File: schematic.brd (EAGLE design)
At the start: 100 x 80 mm, 24 parts, among them IC1 ATMEGA168-20P, IC2 7805T, IC3 REG1117

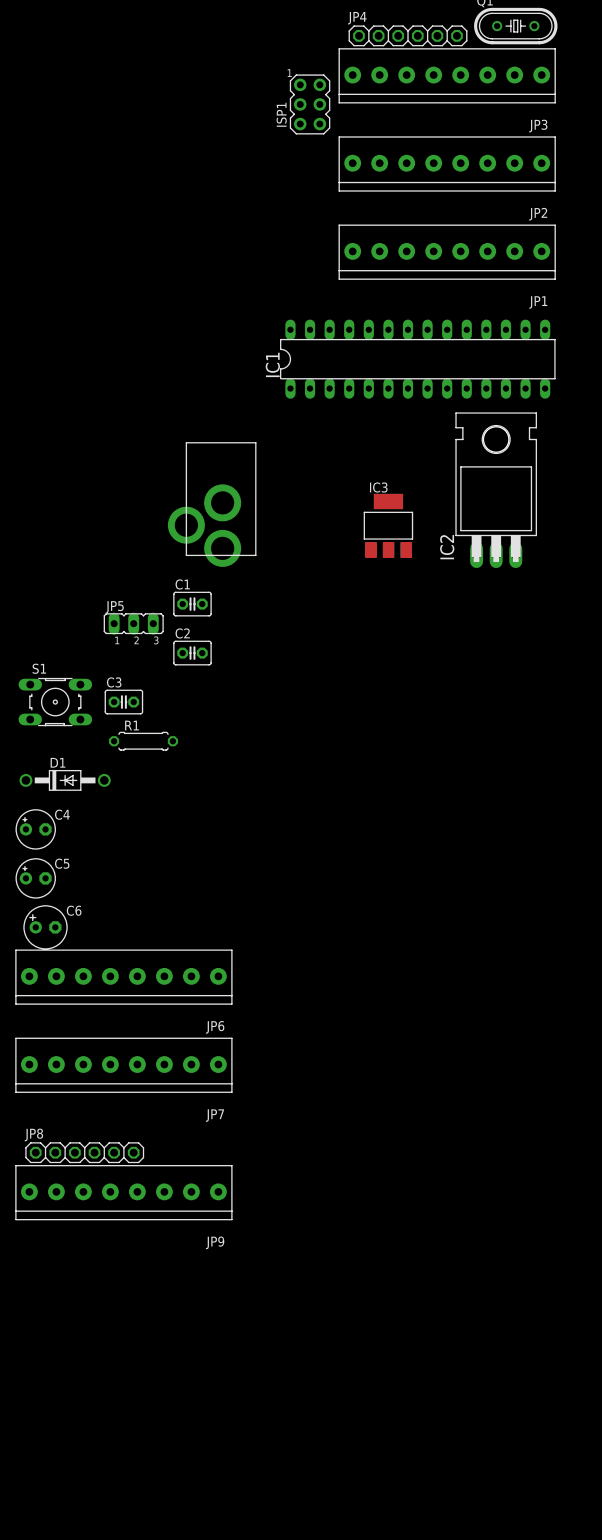
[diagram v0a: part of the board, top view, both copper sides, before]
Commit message: Small fixes
Added a serial port header and LEDs for on and pin 13
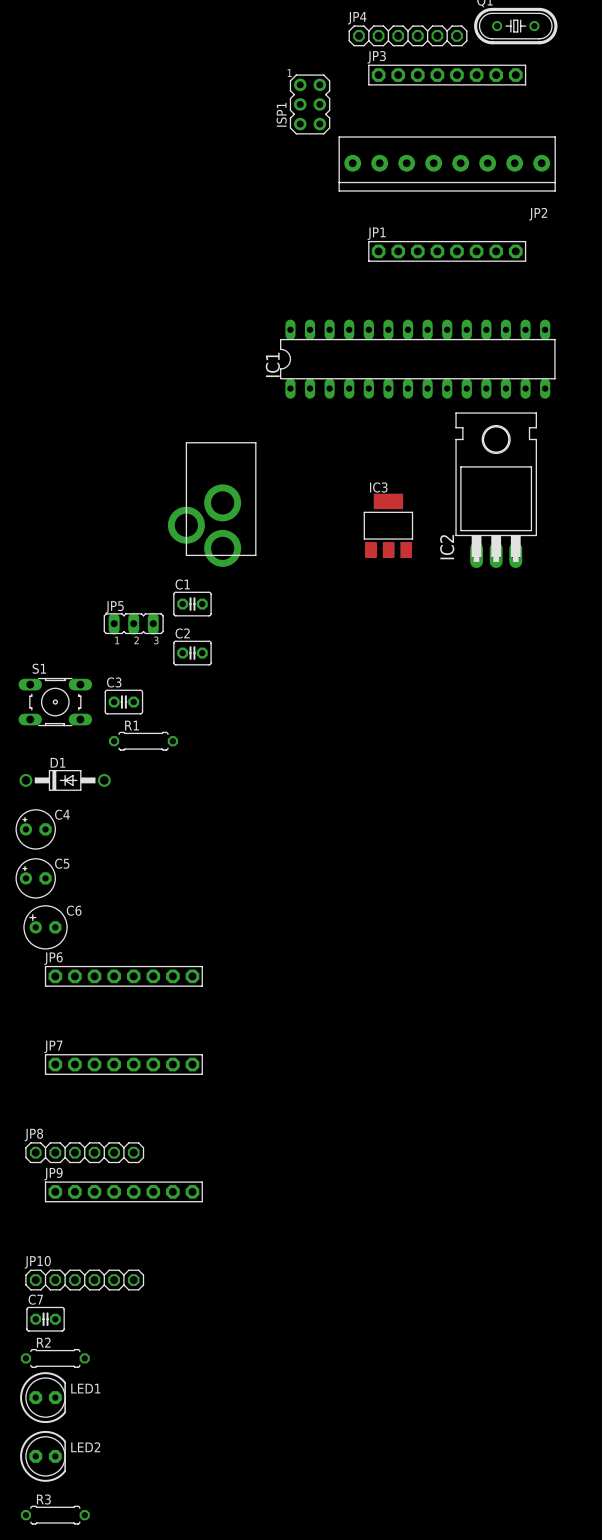
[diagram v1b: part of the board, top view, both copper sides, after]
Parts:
- added C7: (no value), adafruit:C025-030X050
- added JP10: (no value), adafruit:1X06
- added LED1, LED2: (no value), adafruit:LED5MM
- added R2, R3: (no value), rcl:0207/7
- JP1, JP3, JP6, JP7, JP9: device adafruit:1X08-3.5MM -> adafruit:1X08-BIG
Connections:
- removed net N$26: IC1.19, ISP1.3, JP2.6, JP7.6
- new net LED13: IC1.19, ISP1.3, JP2.6, JP7.6, R3.2
- new net N$1: C7.1, JP10.1
- new net N$5: LED1.A, R2.1
- new net N$6: LED2.A, R3.1
- net GND: now also JP10.6, LED1.K, LED2.K
- net N$13: now also JP10.3
- net N$14: now also JP10.2
- net RESET: now also C7.2
- net VCC: now also JP10.4, R2.2

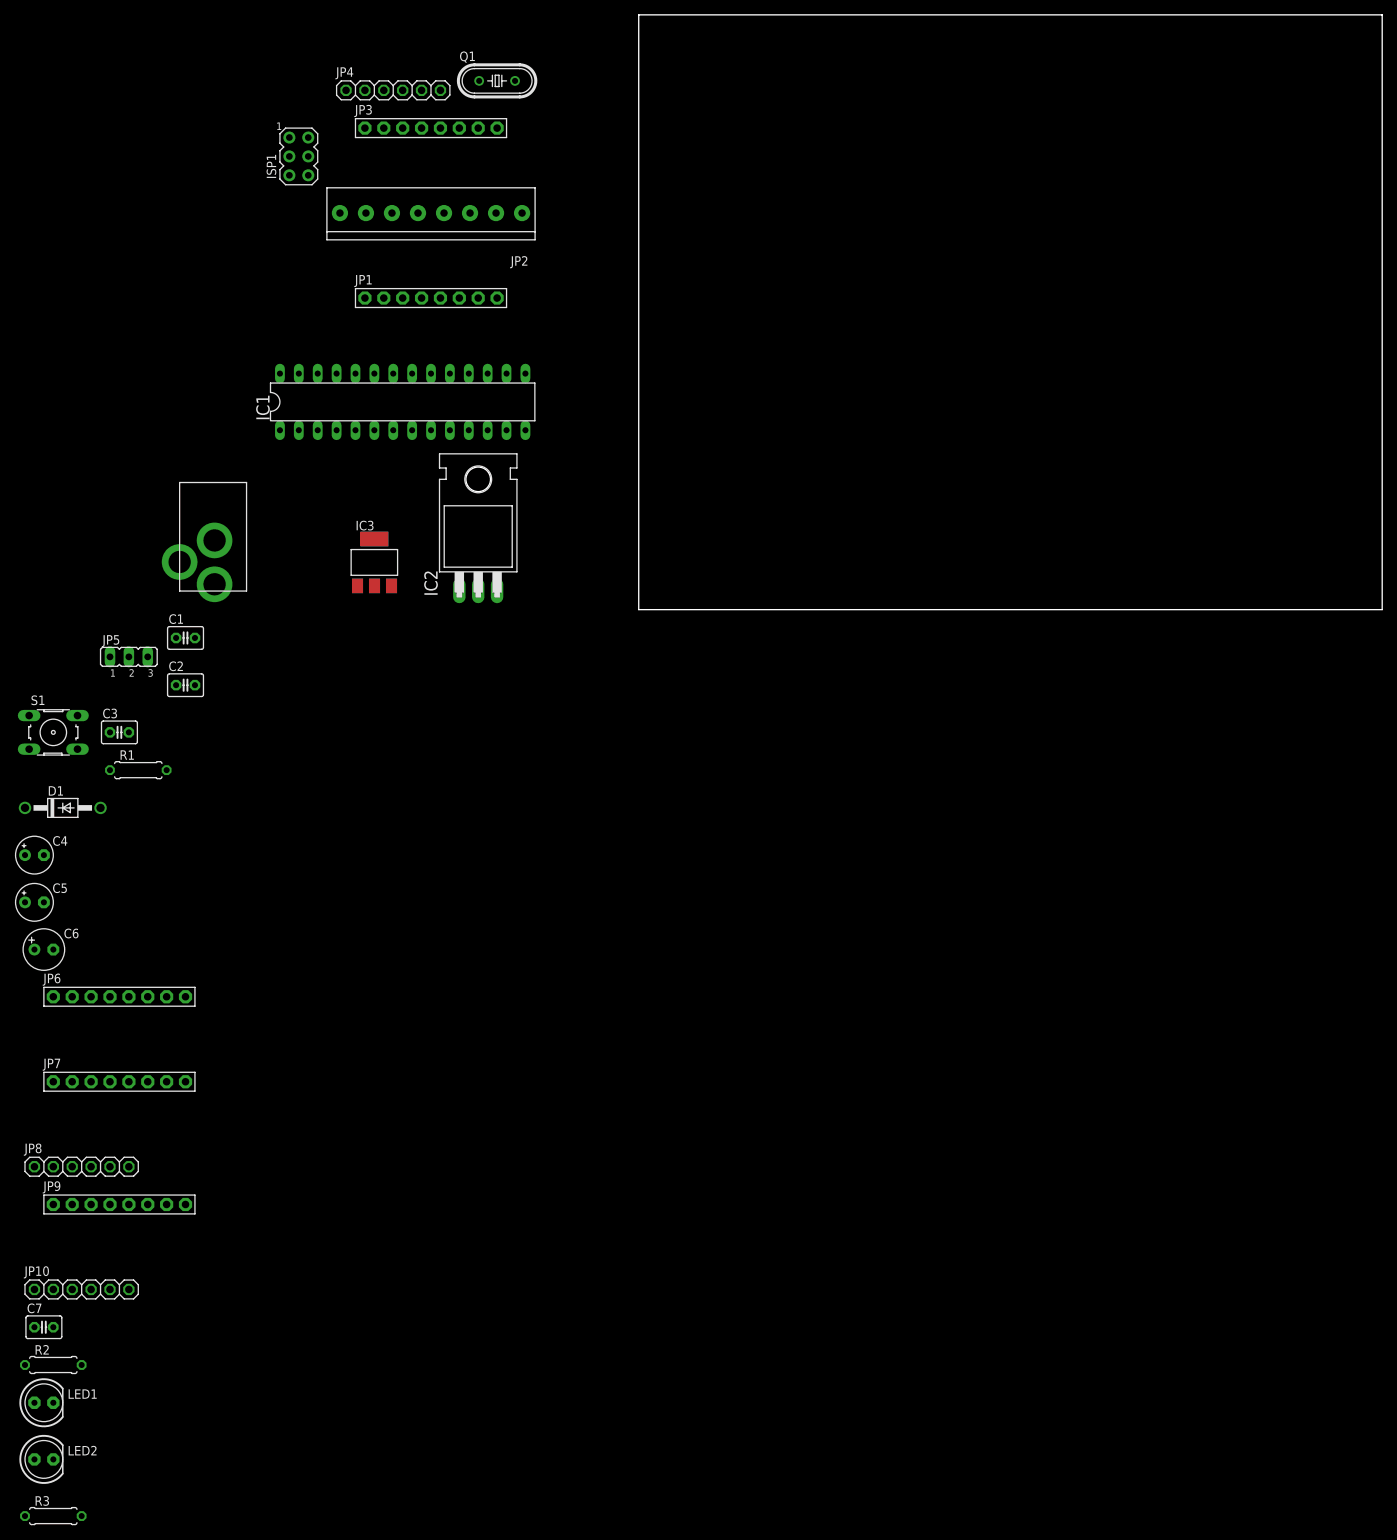
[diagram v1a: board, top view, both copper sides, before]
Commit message: Fixes in net names and the voltage input jack
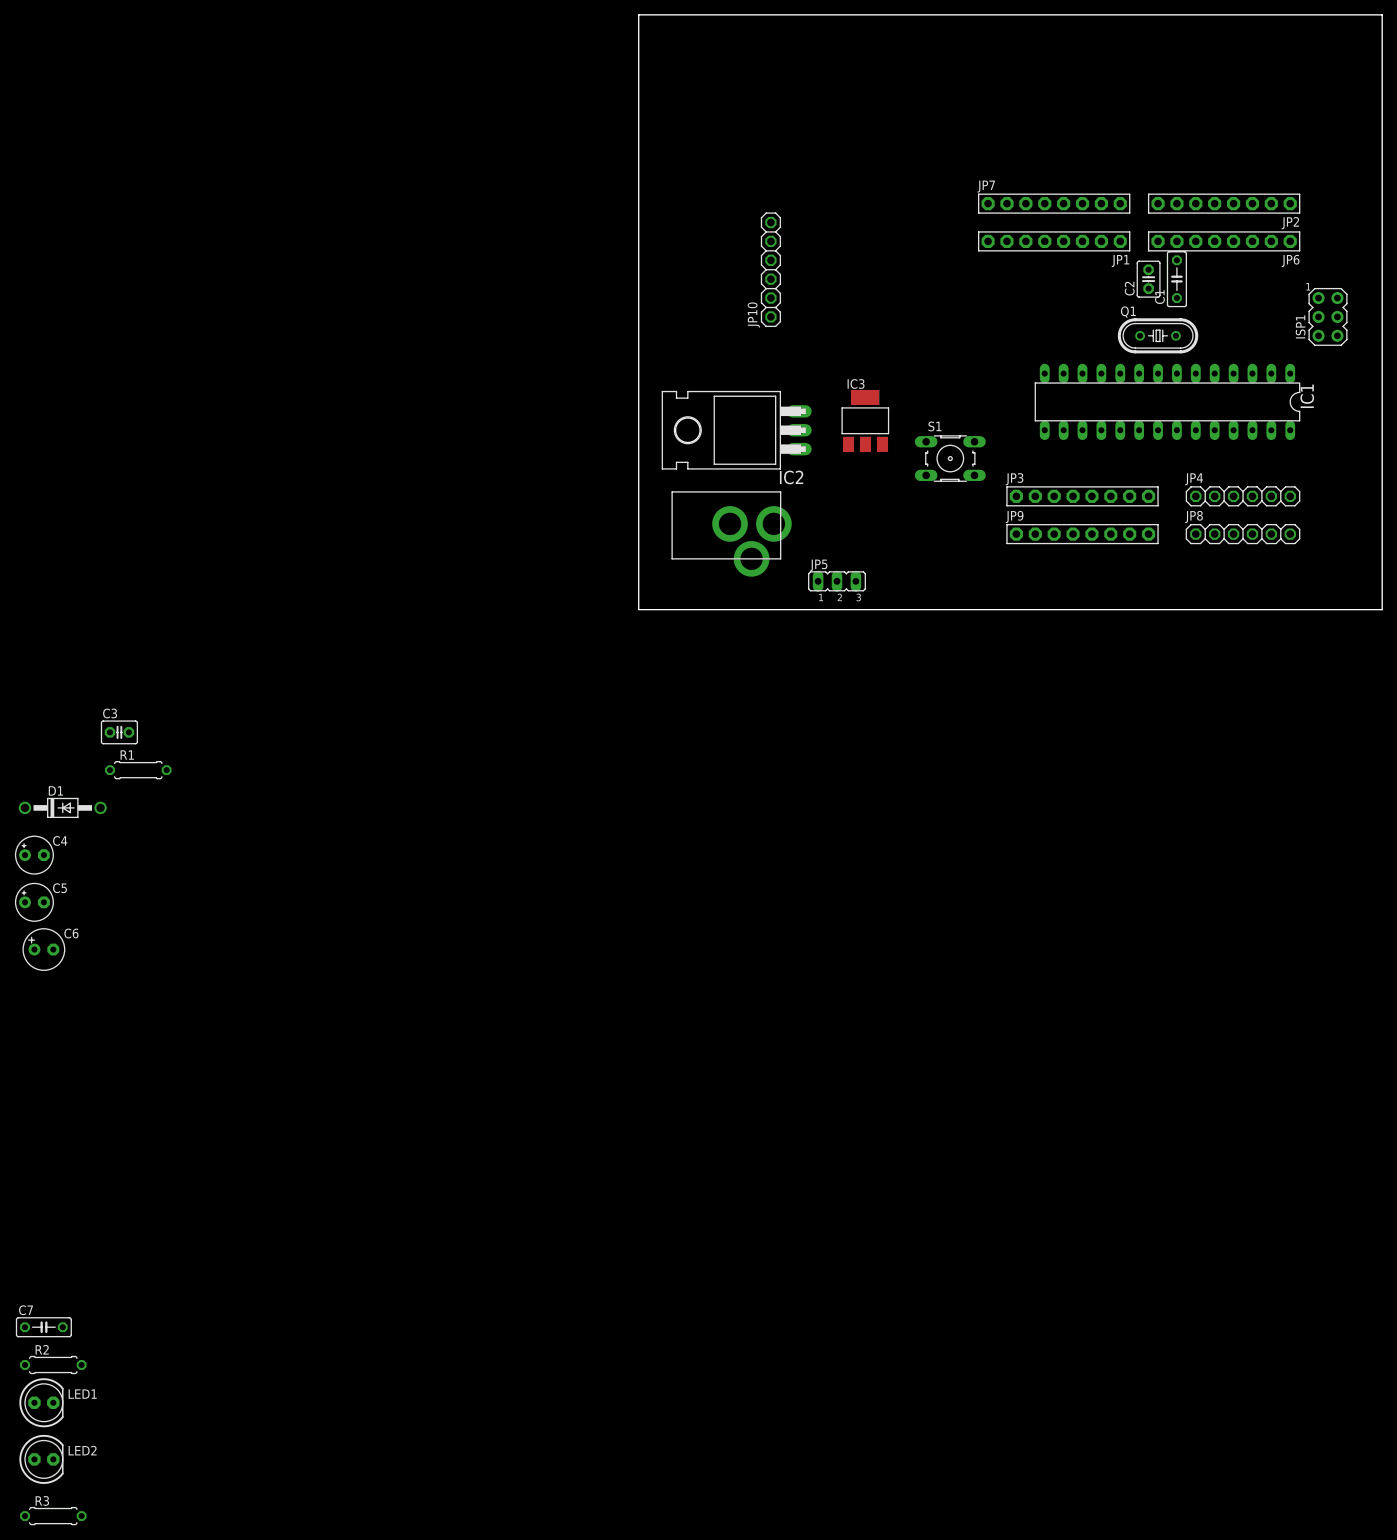
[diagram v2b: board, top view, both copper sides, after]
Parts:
- C1, C7: device adafruit:C025-030X050 -> resistor:C050-025X075
- JP2: device adafruit:1X08-3.5MM -> adafruit:1X08-BIG
- moved JP6 180.0 mm to (78.7, 49.5), turned to 180 degrees
- moved JP8 177.9 mm to (81.3, 10.2)
- moved JP7 172.5 mm to (55.9, 54.6)
- moved JP10 165.6 mm to (17.8, 45.7), turned to 90 degrees
- moved JP9 157.8 mm to (59.7, 10.2)
- moved C1 141.8 mm to (72.4, 44.5), turned to 90 degrees
- moved C2 140.6 mm to (68.6, 44.5), turned to 90 degrees
- moved ISP1 140.1 mm to (92.7, 39.4)
- moved JP4 126.7 mm to (81.3, 15.2)
- moved S1 126.1 mm to (41.9, 20.3)
- moved JP2 106.7 mm to (78.7, 54.6), turned to 180 degrees
- moved IC1 102.9 mm to (71.1, 27.9), turned to 180 degrees
- moved JP3 100.7 mm to (59.7, 15.2)
- moved JP5 95.8 mm to (26.7, 3.81)
- moved Q1 95.3 mm to (69.8, 36.8)
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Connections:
- removed net N$4: IC1.20, IC1.7
- new net VD: C6.+, D1.C, IC2.1, IC3.3
- net GND: now also U$1.RING, U$1.RING_SW; no longer U$1.TIP
- net VCC: now also IC1.20, IC1.7
- net VIN: now also U$1.TIP; no longer C6.+, D1.C, IC2.1, IC3.3, U$1.RING, U$1.RING_SW

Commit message: Fixed some things in schematic and started working on layout
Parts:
- JP4, JP8: device adafruit:1X06 -> adafruit:1X06-BIG
- moved R3 208.8 mm to (45.7, 45.7), turned to 90 degrees
- moved R2 201.9 mm to (92.7, 5.08)
- moved LED2 193.7 mm to (29.2, 45.7)
- moved LED1 191.3 mm to (35.6, 45.7)
- moved C7 168.0 mm to (35.6, 25.4), turned to 90 degrees
- moved R1 162.8 mm to (88.9, 24.1)
- moved C3 157.7 mm to (85.1, 12.7)
- moved C4 134.0 mm to (33.0, 36.8)
- moved C5 132.1 mm to (26.7, 36.8)
- moved C6 126.8 mm to (30.5, 16.5), turned to 270 degrees
- moved D1 110.1 mm to (25.4, 12.7), turned to 270 degrees
- moved JP5 51.2 mm to (20.3, 54.6)
- moved JP2 37.1 mm to (41.7, 55.9)
- moved S1 32.4 mm to (63.5, 44.5)
- moved IC3 20.1 mm to (19.1, 41.9)
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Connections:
- new net N$4: JP3.5, JP9.5
- net +5V: no longer JP3.5, JP9.5

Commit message: Finished layout, still needs cleaning
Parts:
- JP3: device adafruit:1X08-BIG -> adafruit:1X06-BIG
- LED1, LED2: device adafruit:LED5MM -> adafruit:LED3MM
- moved R2 85.4 mm to (19.1, 48.3), turned to 180 degrees
- moved C3 38.7 mm to (55.9, 38.1)
- moved JP5 35.9 mm to (15.2, 19.1), turned to 180 degrees
- moved C7 34.1 mm to (20.3, 55.9), turned to 0 degrees
- moved C2 27.4 mm to (50.8, 38.1), turned to 0 degrees
- moved R3 26.8 mm to (19.1, 43.2), turned to 180 degrees
- moved C1 23.4 mm to (57.1, 43.2), turned to 0 degrees
- moved R1 20.5 mm to (69.8, 31.8), turned to 180 degrees
- moved ISP1 19.1 mm to (73.7, 38.1)
- moved C4 10.2 mm to (22.9, 36.8), turned to 90 degrees
- moved LED1 9.25 mm to (26.7, 48.3)
- moved IC3 7.18 mm to (14.0, 36.8), turned to 90 degrees
- moved S1 6.48 mm to (64.8, 38.1), turned to 270 degrees
- moved C6 5.08 mm to (30.5, 11.4)
- moved JP10 5.08 mm to (12.7, 49.5), turned to 270 degrees
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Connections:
- removed net N$4: JP3.5, JP9.5
- net +3V3: now also JP3.2; no longer JP3.4
- net +5V: now also JP3.3, JP9.5
- net GND: now also JP3.4, JP3.5; no longer JP3.6, JP3.7
- net RESET: now also JP3.1; no longer JP3.3
- net VIN: now also JP3.6; no longer JP3.8
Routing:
- net GND: track 0.00 -> 291.3 mm, vias 0 -> 1
- net RESET: track 0.00 -> 139.2 mm, vias 0 -> 2
- net VCC: track 0.00 -> 139.2 mm, vias 0 -> 3
- net LED13: track 0.00 -> 113.4 mm, vias 0 -> 1
- net N$25: track 0.00 -> 96.6 mm, vias 0 -> 1
- net +3V3: track 0.00 -> 93.2 mm, vias 0 -> 1
- net N$13: track 0.00 -> 92.3 mm
- net N$14: track 0.00 -> 89.0 mm
- net N$24: track 0.00 -> 87.2 mm, vias 0 -> 2
- net +5V: track 0.00 -> 63.6 mm, vias 0 -> 1
- net AREF: track 0.00 -> 61.7 mm
- net VIN: track 0.00 -> 49.8 mm
- net N$23: track 0.00 -> 43.2 mm, vias 0 -> 1
- net VD: track 0.00 -> 40.0 mm, vias 0 -> 1
- net N$22: track 0.00 -> 39.9 mm
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
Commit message: No drc errors
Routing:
- net +3V3: track 93.2 -> 77.3 mm, vias 1 -> 2
- net VCC: track 139.2 -> 154.9 mm, vias 3 -> 2
- net GND: track 291.3 -> 278.5 mm
- net VD: track 40.0 -> 43.1 mm, vias 1 -> 0
- net +5V: track 63.6 -> 62.8 mm
- net VIN: vias 0 -> 1

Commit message: First version
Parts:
- removed JP10: (no value), adafruit:1X06
- added SERIAL: (no value), adafruit:1X06
- C1, C7: value (none) -> 100nF
- C2, C3: value (none) -> 22pF
- C4, C5: value (none) -> 10uF
- C6: value (none) -> 47uF
- R1: value (none) -> 10k
- R2, R3: value (none) -> 1k
- XTAL: value (none) -> 16M
- moved C7 2.54 mm to (22.9, 55.9)
- renumbered IC1 to ATMEGA, IC2 to REG5, IC3 to REG33, ISP1 to ISP, JP5 to 3.3-5V, LED1 to POWER, LED2 to LED13, Q1 to XTAL, S1 to RESET, U$1 to IN
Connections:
- net GND: now also SERIAL.6; no longer JP10.6
- net N$1: now also SERIAL.1; no longer JP10.1
- net N$13: now also SERIAL.3; no longer JP10.3
- net N$14: now also SERIAL.2; no longer JP10.2
- net VCC: now also SERIAL.4; no longer JP10.4
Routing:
- net N$1: track 5.08 -> 11.4 mm
- net N$14: track 89.0 -> 92.8 mm
- net N$13: track 92.3 -> 96.1 mm
- net GND: track 278.5 -> 275.7 mm
- net RESET: track 139.2 -> 136.7 mm
- net VCC: track 154.9 -> 157.1 mm
- net +3V3: track 77.3 -> 76.5 mm
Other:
- board text added: "10"
- board text added: "11"
- board text added: "12"
- board text added: "13"
- board text added: "2"
- board text added: "3"
- board text added: "3.3V"
- board text added: "4"
- board text added: "5"
- board text added: "5V"
- board text added: "6"
- board text added: "7"
- board text added: "8"
- board text added: "9"
- board text added: "A0"
- board text added: "A1"
- board text added: "A2"
- board text added: "A3"
- board text added: "A4"
- board text added: "A5"
- board text added: "AREF"
- board text added: "DTR"
- board text added: "GND"
- board text added: "RST"
- board text added: "RX"
- board text added: "RX 0"
- board text added: "TX"
- board text added: "TX 1"
- board text added: "VCC"
- board text added: "Vin"
- board text added: "dragaosemchama.com.br"
